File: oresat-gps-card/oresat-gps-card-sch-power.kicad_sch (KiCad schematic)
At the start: 95 parts, among them Q1 DMP2240UDM, Q2 PMV45EN, Q3 DMP3050LVT-7, Q4 DMP3050LVT-7, Q5 PMV45EN, U2 MAX7310ATE, U3 MIC842LYC5, U4 MIC842LYC5, U5 MAX4211FETE, U6 LTC3624, U7 TS5A21366

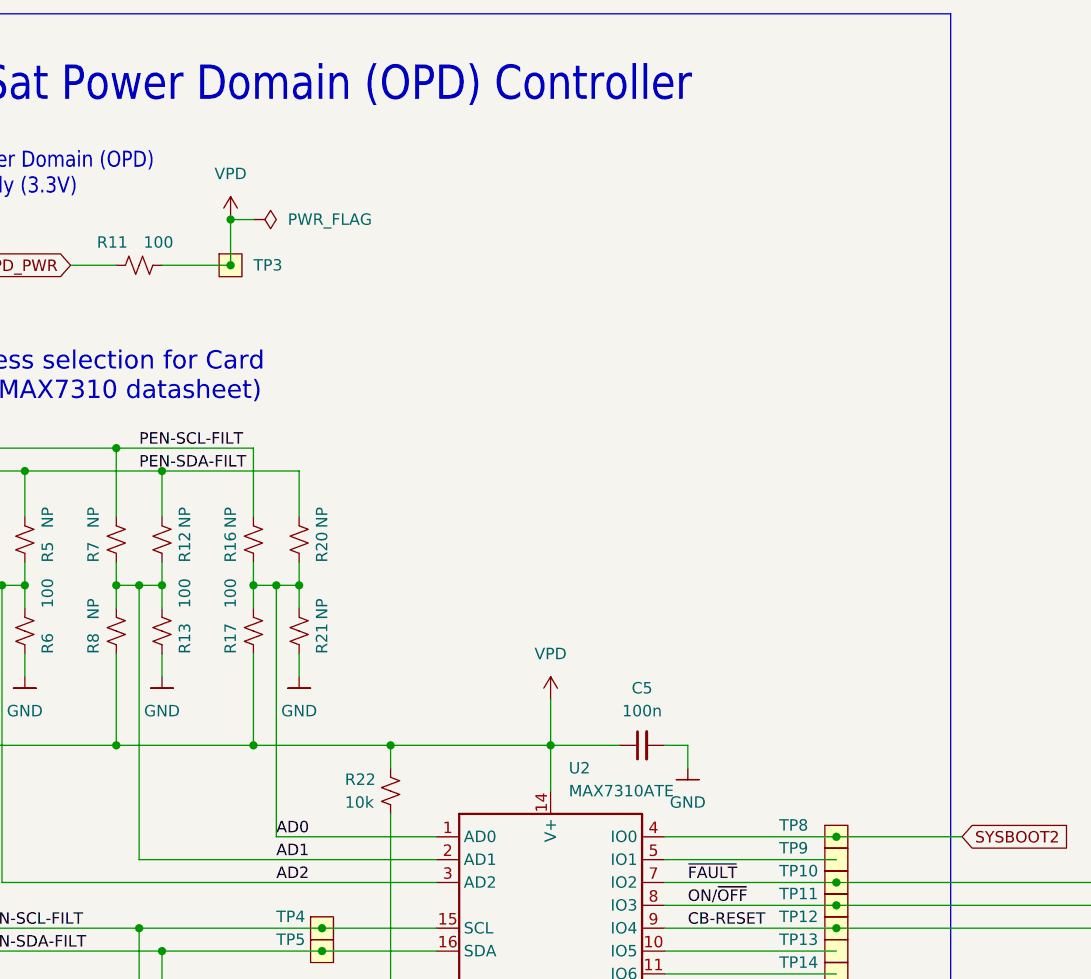
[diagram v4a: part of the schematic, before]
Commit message: Update RF path for sunstone board run, and connected VPD diodes
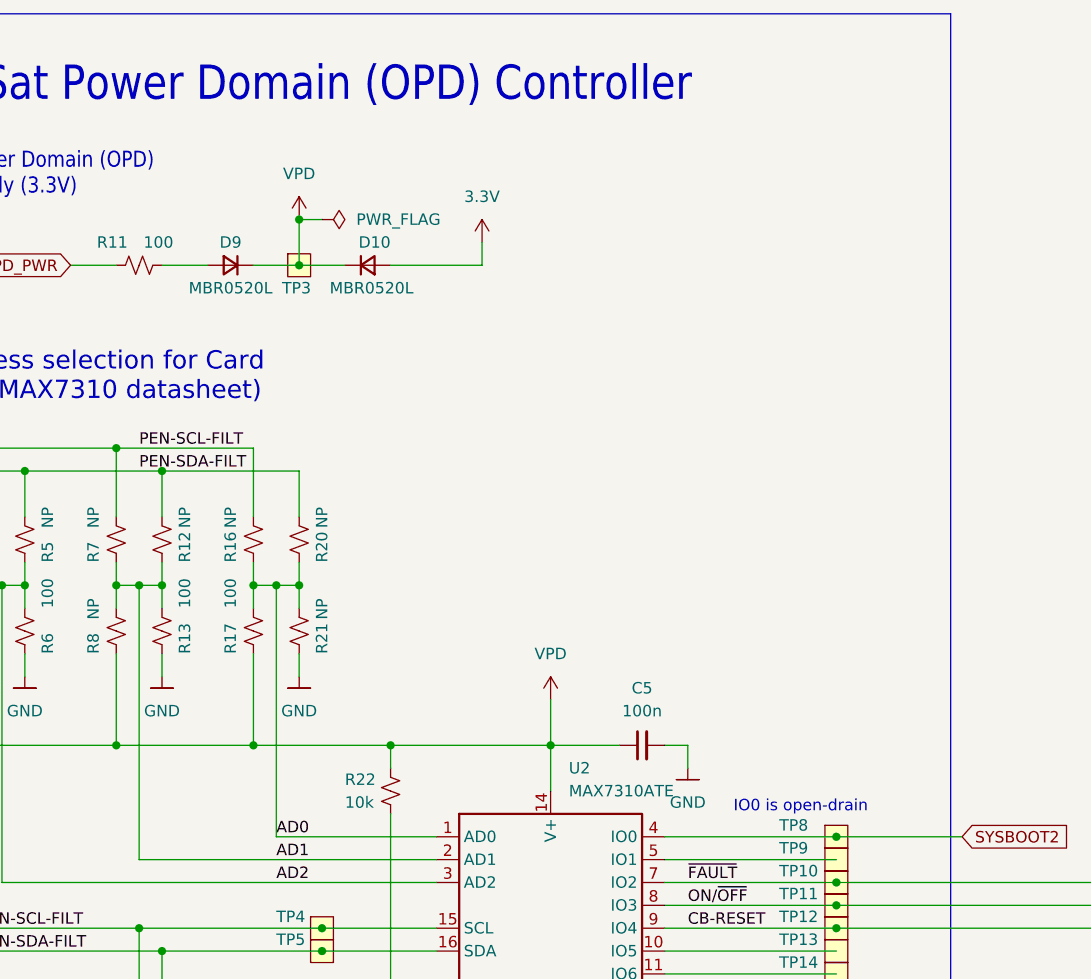
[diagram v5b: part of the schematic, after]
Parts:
- added D10, D9: MBR0520L, Diode_SMD:D_SOD-123, symbol Device:D_Small
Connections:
- net VPD: now also D10.1 (K), D9.1 (K); no longer R11.2
- new net: D9.2 (A), R11.2
- new net 3.3V: D10.2 (A)
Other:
- note added: "IO0 is open-drain"
- moved on the sheet: TP3
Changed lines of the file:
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@@
   (junction (at 147.32 127) (diameter 0) (color 0 0 0 0)
   )
-  (junction (at 73.66 45.72) (diameter 0) (color 0 0 0 0)
+  (junction (at 81.28 45.72) (diameter 0) (color 0 0 0 0)
   )
   (junction (at 309.88 68.58) (diameter 0) (color 0 0 0 0)
@@
   (junction (at 71.12 223.52) (diameter 0) (color 0 0 0 0)
   )
-  (junction (at 73.66 40.64) (diameter 0) (color 0 0 0 0)
+  (junction (at 81.28 40.64) (diameter 0) (color 0 0 0 0)
   )
   (junction (at 71.12 175.26) (diameter 0) (color 0 0 0 0)
@@
     (stroke (width 0) (type default))
   )
+  (wire (pts (xy 76.2 45.72) (xy 81.28 45.72))
+    (stroke (width 0) (type default))
+  )
   (wire (pts (xy 375.92 43.18) (xy 375.92 48.26))
     (stroke (width 0) (type default))
@@
     (stroke (width 0) (type default))
   )
+  (wire (pts (xy 81.28 45.72) (xy 86.36 45.72))
+    (stroke (width 0) (type default))
+  )
   (wire (pts (xy 203.2 50.8) (xy 203.2 55.88))
     (stroke (width 0) (type default))
@@
     (stroke (width 0) (type default))
   )
-  (wire (pts (xy 66.04 45.72) (xy 73.66 45.72))
+  (wire (pts (xy 66.04 45.72) (xy 71.12 45.72))
     (stroke (width 0) (type default))
   )
@@
     (stroke (width 0) (type default))
   )
+  (wire (pts (xy 91.44 45.72) (xy 101.6 45.72))
+    (stroke (width 0) (type default))
+  )
   (wire (pts (xy 60.96 78.74) (xy 60.96 81.28))
     (stroke (width 0) (type default))
@@
     (stroke (width 0) (type default))
   )
+  (wire (pts (xy 101.6 45.72) (xy 101.6 43.18))
+    (stroke (width 0) (type default))
+  )
   (wire (pts (xy 121.92 111.76) (xy 140.97 111.76))
     (stroke (width 0) (type default))
@@
     (stroke (width 0) (type default))
   )
-  (wire (pts (xy 73.66 40.64) (xy 76.2 40.64))
+  (wire (pts (xy 81.28 40.64) (xy 83.82 40.64))
     (stroke (width 0) (type default))
   )
@@
     (stroke (width 0) (type default))
   )
-  (wire (pts (xy 73.66 40.64) (xy 73.66 45.72))
+  (wire (pts (xy 81.28 40.64) (xy 81.28 45.72))
     (stroke (width 0) (type default))
   )
@@
     (effects (font (size 3.81 3.2385)) (justify left bottom))
   )
+  (text "IO0 is open-drain" (at 129.54 106.68 0)
+    (effects (font (size 1.27 1.27)) (justify left bottom))
+  )
   (text "OreSat Power Domain (OPD)\nPower Supply (3.3V)" (at 35.56 38.1 0)
     (effects (font (size 1.778 1.5113)) (justify left bottom))
@@
     )
   )
-  (symbol (lib_id "oresat-power:VPD") (at 73.66 40.64 0) (unit 1)
+  (symbol (lib_id "oresat-power:VPD") (at 81.28 40.64 0) (unit 1)
     (in_bom yes) (on_board yes) (dnp no) (fields_autoplaced)
-    (property "Reference" "#VPD0104" (at 73.66 44.45 0)
+    (property "Reference" "#VPD0104" (at 81.28 44.45 0)
       (effects (font (size 1.27 1.27)) hide)
     )
-    (property "Value" "VPD" (at 73.66 35.56 0)
+    (property "Value" "VPD" (at 81.28 35.56 0)
       (effects (font (size 1.27 1.27)))
     )
-    (property "Footprint" "" (at 73.66 40.64 0)
+    (property "Footprint" "" (at 81.28 40.64 0)
       (effects (font (size 1.27 1.27)) hide)
     )
-    (property "Datasheet" "" (at 73.66 40.64 0)
+    (property "Datasheet" "" (at 81.28 40.64 0)
       (effects (font (size 1.27 1.27)) hide)
     )
@@
     )
   )
-  (symbol (lib_id "power:PWR_FLAG") (at 76.2 40.64 270) (unit 1)
+  (symbol (lib_id "power:PWR_FLAG") (at 83.82 40.64 270) (unit 1)
     (in_bom yes) (on_board yes) (dnp no) (fields_autoplaced)
-    (property "Reference" "#FLG01" (at 78.105 40.64 0)
+    (property "Reference" "#FLG01" (at 85.725 40.64 0)
       (effects (font (size 1.27 1.27)) hide)
     )
-    (property "Value" "PWR_FLAG" (at 80.01 40.64 90)
+    (property "Value" "PWR_FLAG" (at 87.63 40.64 90)
       (effects (font (size 1.27 1.27)) (justify left))
     )
-    (property "Footprint" "" (at 76.2 40.64 0)
+    (property "Footprint" "" (at 83.82 40.64 0)
       (effects (font (size 1.27 1.27)) hide)
     )
-    (property "Datasheet" "~" (at 76.2 40.64 0)
+    (property "Datasheet" "~" (at 83.82 40.64 0)
       (effects (font (size 1.27 1.27)) hide)
     )
@@
     )
   )
-  (symbol (lib_id "oresat-misc:Test-Point-0.75mm-th") (at 73.66 45.72 0) (unit 1)
+  (symbol (lib_id "oresat-misc:Test-Point-0.75mm-th") (at 81.28 45.72 0) (unit 1)
     (in_bom yes) (on_board yes) (dnp no)
-    (property "Reference" "TP3" (at 76.2 45.72 0)
+    (property "Reference" "TP3" (at 79.375 48.26 0)
       (effects (font (size 1.27 1.27)) (justify left))
     )
-    (property "Value" "1x01" (at 73.66 43.18 0)
+    (property "Value" "1x01" (at 81.28 43.18 0)
       (effects (font (size 1.27 1.27)) hide)
     )
-    (property "Footprint" "oresat-misc:TestPoint-0.75mm-th" (at 73.66 43.18 0)
+    (property "Footprint" "oresat-misc:TestPoint-0.75mm-th" (at 81.28 43.18 0)
       (effects (font (size 1.27 1.27)) hide)
     )
-    (property "Datasheet" "" (at 73.66 43.18 0)
+    (property "Datasheet" "" (at 81.28 43.18 0)
       (effects (font (size 1.27 1.27)) hide)
     )
@@
     )
   )
+  (symbol (lib_id "Device:D_Small") (at 88.9 45.72 0) (unit 1)
+    (in_bom yes) (on_board yes) (dnp no)
+    (property "Reference" "D10" (at 91.44 43.18 0)
+      (effects (font (size 1.27 1.27)) (justify right))
+    )
+    (property "Value" "MBR0520L" (at 93.98 48.26 0)
+      (effects (font (size 1.27 1.27)) (justify right))
+    )
+    (property "Footprint" "Diode_SMD:D_SOD-123" (at 88.9 45.72 90)
+      (effects (font (size 1.27 1.27)) hide)
+    )
+    (property "Datasheet" "~" (at 88.9 45.72 90)
+      (effects (font (size 1.27 1.27)) hide)
+    )
+    (property "Sim.Device" "D" (at 88.9 45.72 0)
+      (effects (font (size 1.27 1.27)) hide)
+    )
+    (property "Sim.Pins" "1=K 2=A" (at 88.9 45.72 0)
+      (effects (font (size 1.27 1.27)) hide)
+    )
+    (pin "1")
+    (pin "2")
+    (instances
+      (project "oresat-gps-card"
+        (path "/65d12cdd-c326-4033-9053-c59fa4e0b25e/0c1da208-2d1c-4d05-9cc7-59584e50a6ac"
+          (reference "D10") (unit 1)
+        )
+        (path "/65d12cdd-c326-4033-9053-c59fa4e0b25e/2134bb9a-062c-4e32-a41e-d15ce3545372"
+          (reference "D10") (unit 1)
+        )
+      )
+    )
+  )
   (symbol (lib_id "oresat-power:GND") (at 99.06 218.44 0) (unit 1)
     (in_bom yes) (on_board yes) (dnp no) (fields_autoplaced)
@@
     )
   )
+  (symbol (lib_id "oresat-power:3.3V") (at 101.6 43.18 0) (unit 1)
+    (in_bom yes) (on_board yes) (dnp no) (fields_autoplaced)
+    (property "Reference" "#3V0113" (at 101.6 46.99 0)
+      (effects (font (size 1.27 1.27)) hide)
+    )
+    (property "Value" "3.3V" (at 101.6 38.1 0)
+      (effects (font (size 1.27 1.27)))
+    )
+    (property "Footprint" "" (at 101.6 43.18 0)
+      (effects (font (size 1.27 1.27)) hide)
+    )
+    (property "Datasheet" "" (at 101.6 43.18 0)
+      (effects (font (size 1.27 1.27)) hide)
+    )
+    (pin "1")
+    (instances
+      (project "oresat-gps-card"
+        (path "/65d12cdd-c326-4033-9053-c59fa4e0b25e/0c1da208-2d1c-4d05-9cc7-59584e50a6ac"
+          (reference "#3V0113") (unit 1)
+        )
+        (path "/65d12cdd-c326-4033-9053-c59fa4e0b25e/2134bb9a-062c-4e32-a41e-d15ce3545372"
+          (reference "#3V02") (unit 1)
+        )
+      )
+    )
+  )
   (symbol (lib_id "oresat-misc:Test-Point-0.75mm-th") (at 261.62 104.14 0) (unit 1)
     (in_bom yes) (on_board yes) (dnp no)
@@
         )
       )
+    )
+  )
+  (symbol (lib_id "Device:D_Small") (at 73.66 45.72 180) (unit 1)
+    (in_bom yes) (on_board yes) (dnp no)
+    (property "Reference" "D9" (at 73.66 43.18 0)
+      (effects (font (size 1.27 1.27)))
+    )
+    (property "Value" "MBR0520L" (at 73.66 48.26 0)
+      (effects (font (size 1.27 1.27)))
+    )
+    (property "Footprint" "Diode_SMD:D_SOD-123" (at 73.66 45.72 90)
+      (effects (font (size 1.27 1.27)) hide)
+    )
+    (property "Datasheet" "~" (at 73.66 45.72 90)
+      (effects (font (size 1.27 1.27)) hide)
+    )
+    (property "Sim.Device" "D" (at 73.66 45.72 0)
+      (effects (font (size 1.27 1.27)) hide)
+    )
+    (property "Sim.Pins" "1=K 2=A" (at 73.66 45.72 0)
+      (effects (font (size 1.27 1.27)) hide)
+    )
+    (pin "1")
+    (pin "2")
+    (instances
+      (project "oresat-gps-card"
+        (path "/65d12cdd-c326-4033-9053-c59fa4e0b25e/0c1da208-2d1c-4d05-9cc7-59584e50a6ac"
+          (reference "D9") (unit 1)
+        )
+        (path "/65d12cdd-c326-4033-9053-c59fa4e0b25e/2134bb9a-062c-4e32-a41e-d15ce3545372"
+          (reference "D9") (unit 1)
+        )
+      )

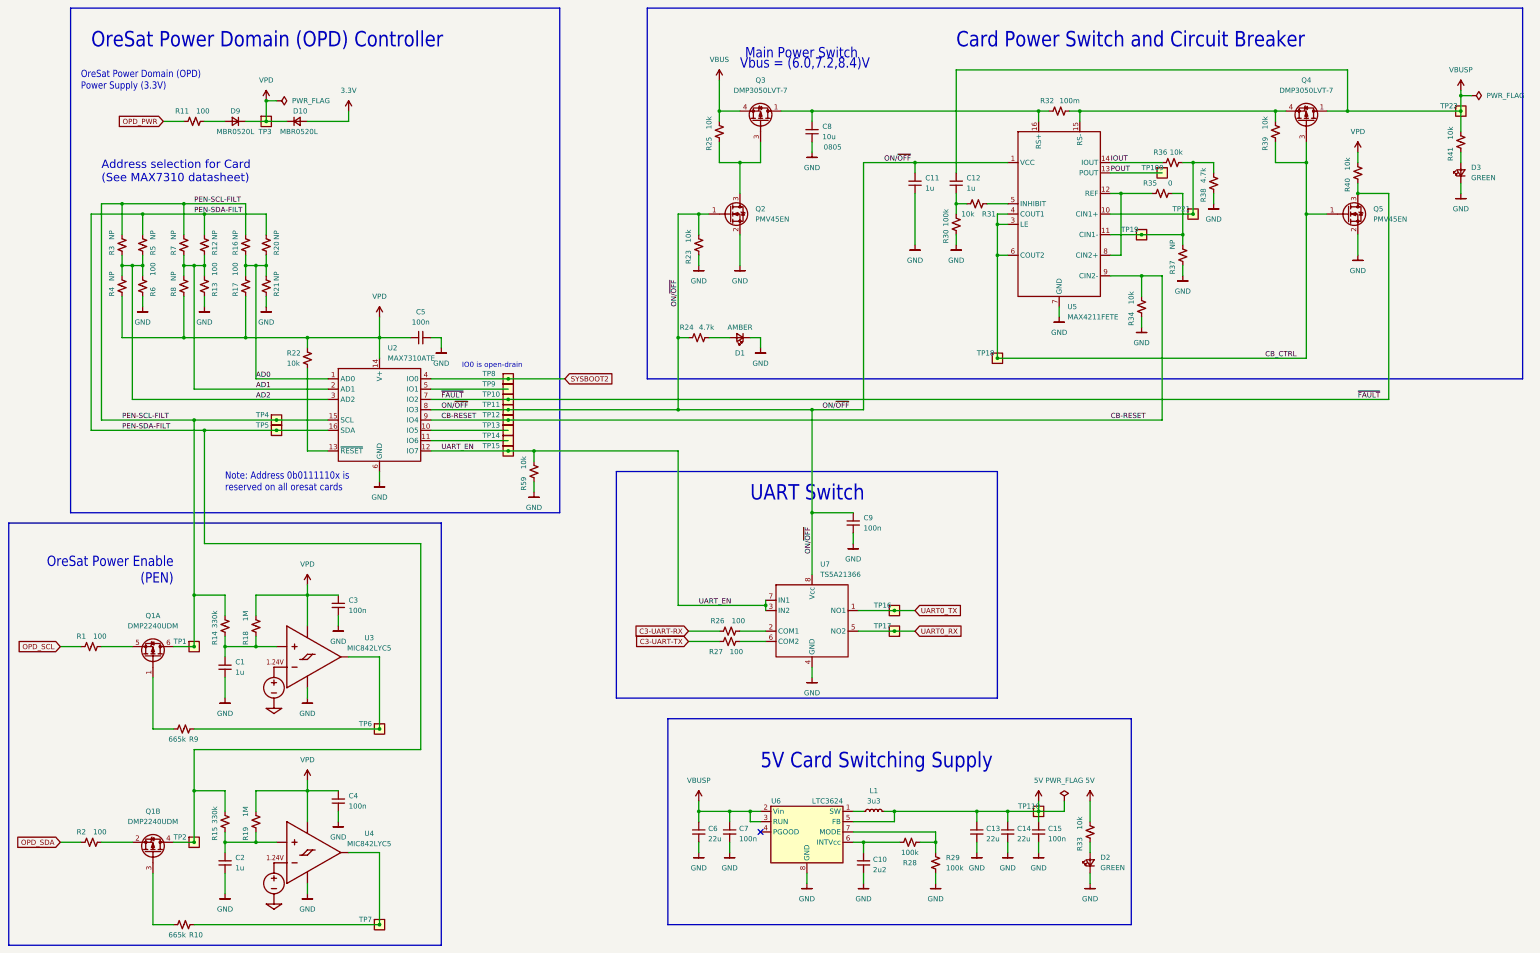
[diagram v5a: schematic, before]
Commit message: Cleaned up ERC and DRC errors on GPS card
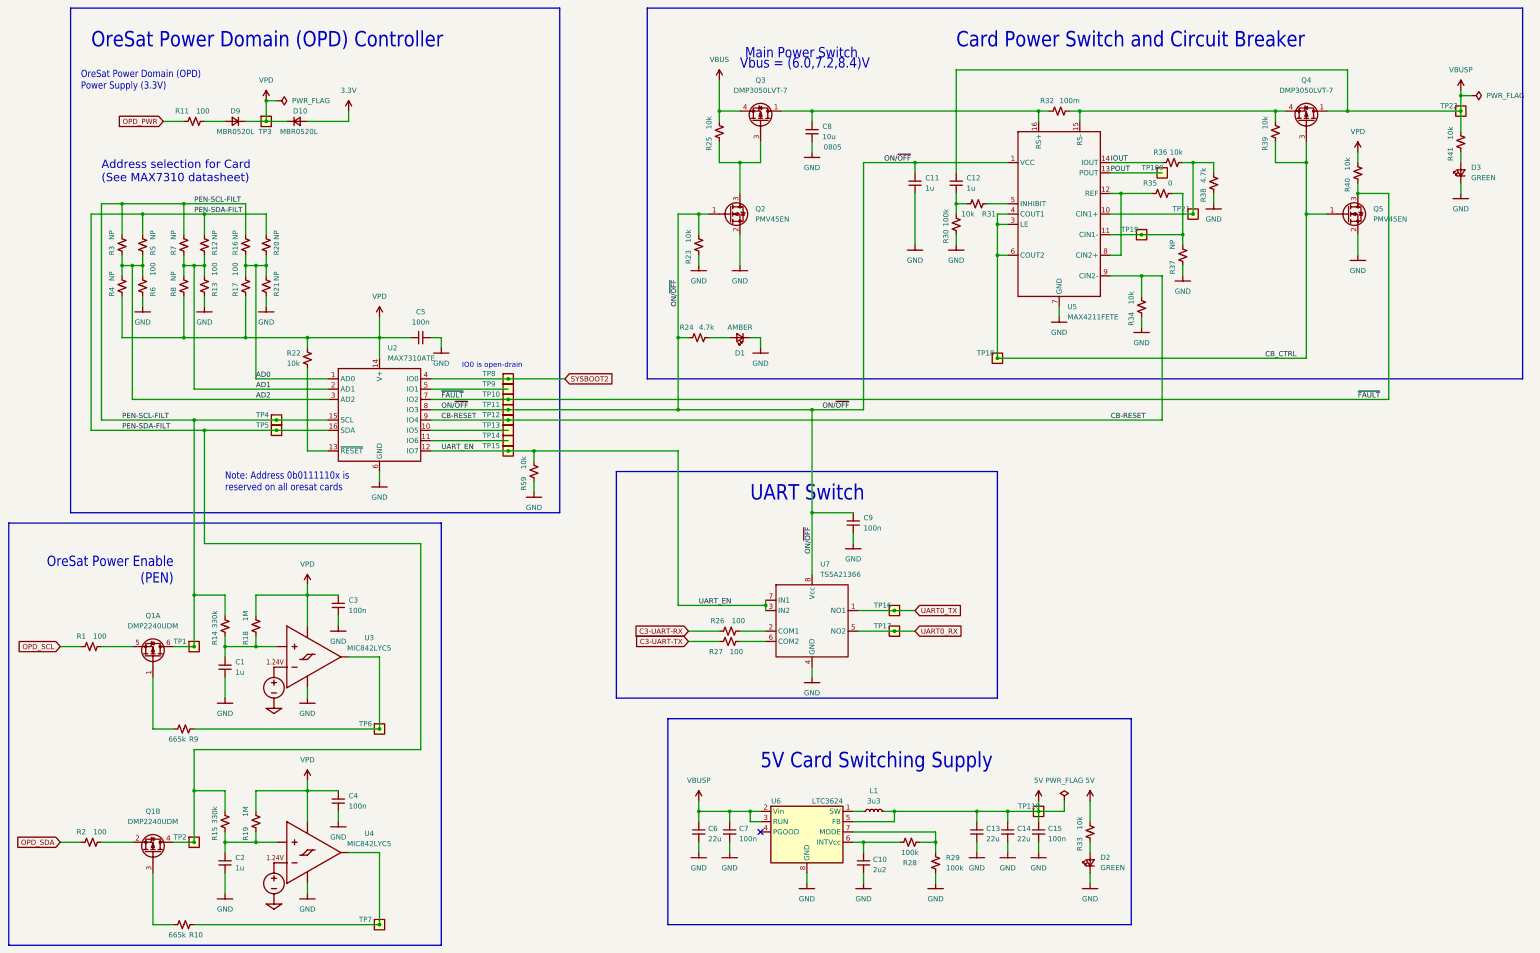
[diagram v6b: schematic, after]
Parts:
- Q2, Q5: footprint oresat-footprints:SOT23 -> oresat-ics:SOT23
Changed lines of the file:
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@@
       (effects (font (size 1.27 1.27)) (justify left))
     )
-    (property "Footprint" "oresat-footprints:SOT23" (at 353.06 66.04 0)
+    (property "Footprint" "oresat-ics:SOT23" (at 353.06 66.04 0)
       (effects (font (size 1.27 1.27)) hide)
     )
@@
       (effects (font (size 1.27 1.27)) (justify left))
     )
-    (property "Footprint" "oresat-footprints:SOT23" (at 200.66 66.04 0)
-      (effects (font (size 1.27 1.27)) hide)
-    )
+    (property "Footprint" "oresat-ics:SOT23" (at 200.66 66.04 0)
+      (effects (font (size 1.27 1.27)) hide)
+    )
